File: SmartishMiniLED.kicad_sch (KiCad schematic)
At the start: 35 parts, among them J1 USB_C_Receptacle_USB2.0, J2 BUTTON, J3 Screw_Terminal_01x03, P1 NeopixelStripPads, P2 NeopixelStripPads, Q1 MMBT2222, Q2 MMBT2222, Q3 IRLML6344, Q4 IRF7410, SW2 TL3342, U1 ESP32-PICO-D4, U2 AP2112K-3.3, U3 CH340C, U4 74LVC1G125, U5 TSOP382xx

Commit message: Added some pads on the back for as an alternative to supplying the main power.
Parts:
- added J4: Conn_01x02, SmartishMiniLED:Main_Power, symbol Connector_Generic:Conn_01x02
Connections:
- net GND: now also J4.2 (Pin_2)
- net +5V_In: now reaches F1.1, J1.A4 (VBUS), J1.A9 (VBUS), J1.B4 (VBUS), J1.B9 (VBUS)
- net +5V_In: now also J4.1 (Pin_1)
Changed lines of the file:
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@@
+    (stroke (width 0) (type default) (color 0 0 0 0))
+  )
+  (wire (pts (xy 49.53 38.1) (xy 49.53 48.26))
     (stroke (width 0) (type default) (color 0 0 0 0))
   )
@@
     (stroke (width 0) (type default) (color 0 0 0 0))
   )
-  (wire (pts (xy 39.37 44.45) (xy 39.37 48.26))
-    (stroke (width 0) (type default) (color 0 0 0 0))
-  )
-  (wire (pts (xy 39.37 29.21) (xy 39.37 26.67))
+  (wire (pts (xy 30.48 45.72) (xy 30.48 49.53))
+    (stroke (width 0) (type default) (color 0 0 0 0))
+  )
+  (wire (pts (xy 30.48 30.48) (xy 30.48 27.94))
     (stroke (width 0) (type default) (color 0 0 0 0))
   )
@@
     (stroke (width 0) (type default) (color 0 0 0 0))
   )
+  (wire (pts (xy 49.53 35.56) (xy 46.99 35.56))
+    (stroke (width 0) (type default) (color 0 0 0 0))
+  )
   (wire (pts (xy 141.605 115.57) (xy 141.605 119.38))
     (stroke (width 0) (type default) (color 0 0 0 0))
   )
-  (wire (pts (xy 29.21 25.4) (xy 29.21 29.21))
+  (wire (pts (xy 20.32 26.67) (xy 20.32 30.48))
     (stroke (width 0) (type default) (color 0 0 0 0))
   )
@@
     (stroke (width 0) (type default) (color 0 0 0 0))
   )
+  (wire (pts (xy 46.99 38.1) (xy 49.53 38.1))
+    (stroke (width 0) (type default) (color 0 0 0 0))
+  )
   (wire (pts (xy 128.27 149.86) (xy 128.27 148.59))
     (stroke (width 0) (type default) (color 0 0 0 0))
@@
   )
   (wire (pts (xy 210.82 133.35) (xy 210.82 135.89))
+    (stroke (width 0) (type default) (color 0 0 0 0))
+  )
+  (wire (pts (xy 49.53 26.67) (xy 49.53 35.56))
     (stroke (width 0) (type default) (color 0 0 0 0))
   )
@@
   (label "RESET" (at 27.94 86.36 180)
     (effects (font (size 1.27 1.27)) (justify right bottom))
+  )
+  (label "+5V_In" (at 49.53 26.67 90)
+    (effects (font (size 1.27 1.27)) (justify left bottom))
+  )
+  (label "+5V_In" (at 201.93 115.57 90)
+    (effects (font (size 1.27 1.27)) (justify left bottom))
   )
   (label "DATA_OUT" (at 223.52 80.01 180)
@@
     (pin "1")
   )
-  (symbol (lib_id "power:PWR_FLAG") (at 39.37 29.21 180) (unit 1)
-    (in_bom yes) (on_board yes)
-    (property "Reference" "#FLG0101" (id 0) (at 39.37 31.115 0)
-      (effects (font (size 1.27 1.27)) hide)
-    )
-    (property "Value" "PWR_FLAG" (id 1) (at 39.37 33.6042 0))
-    (property "Footprint" "" (id 2) (at 39.37 29.21 0)
-      (effects (font (size 1.27 1.27)) hide)
-    )
-    (property "Datasheet" "~" (id 3) (at 39.37 29.21 0)
+  (symbol (lib_id "power:PWR_FLAG") (at 30.48 30.48 180) (unit 1)
+    (in_bom yes) (on_board yes)
+    (property "Reference" "#FLG0101" (id 0) (at 30.48 32.385 0)
+      (effects (font (size 1.27 1.27)) hide)
+    )
+    (property "Value" "PWR_FLAG" (id 1) (at 30.48 34.8742 0))
+    (property "Footprint" "" (id 2) (at 30.48 30.48 0)
+      (effects (font (size 1.27 1.27)) hide)
+    )
+    (property "Datasheet" "~" (id 3) (at 30.48 30.48 0)
       (effects (font (size 1.27 1.27)) hide)
     )
@@
     (pin "1")
   )
-  (symbol (lib_id "power:PWR_FLAG") (at 39.37 44.45 0) (unit 1)
-    (in_bom yes) (on_board yes)
-    (property "Reference" "#FLG0102" (id 0) (at 39.37 42.545 0)
-      (effects (font (size 1.27 1.27)) hide)
-    )
-    (property "Value" "PWR_FLAG" (id 1) (at 39.37 40.0558 0))
-    (property "Footprint" "" (id 2) (at 39.37 44.45 0)
-      (effects (font (size 1.27 1.27)) hide)
-    )
-    (property "Datasheet" "~" (id 3) (at 39.37 44.45 0)
-      (effects (font (size 1.27 1.27)) hide)
-    )
-    (pin "1")
-  )
-  (symbol (lib_id "power:GND") (at 39.37 48.26 0) (unit 1)
-    (in_bom yes) (on_board yes)
-    (property "Reference" "#PWR0123" (id 0) (at 39.37 54.61 0)
-      (effects (font (size 1.27 1.27)) hide)
-    )
-    (property "Value" "GND" (id 1) (at 39.497 52.6542 0))
-    (property "Footprint" "" (id 2) (at 39.37 48.26 0)
-      (effects (font (size 1.27 1.27)) hide)
-    )
-    (property "Datasheet" "" (id 3) (at 39.37 48.26 0)
+  (symbol (lib_id "power:PWR_FLAG") (at 30.48 45.72 0) (unit 1)
+    (in_bom yes) (on_board yes)
+    (property "Reference" "#FLG0102" (id 0) (at 30.48 43.815 0)
+      (effects (font (size 1.27 1.27)) hide)
+    )
+    (property "Value" "PWR_FLAG" (id 1) (at 30.48 41.3258 0))
+    (property "Footprint" "" (id 2) (at 30.48 45.72 0)
+      (effects (font (size 1.27 1.27)) hide)
+    )
+    (property "Datasheet" "~" (id 3) (at 30.48 45.72 0)
+      (effects (font (size 1.27 1.27)) hide)
+    )
+    (pin "1")
+  )
+  (symbol (lib_id "power:GND") (at 30.48 49.53 0) (unit 1)
+    (in_bom yes) (on_board yes)
+    (property "Reference" "#PWR0123" (id 0) (at 30.48 55.88 0)
+      (effects (font (size 1.27 1.27)) hide)
+    )
+    (property "Value" "GND" (id 1) (at 30.607 53.9242 0))
+    (property "Footprint" "" (id 2) (at 30.48 49.53 0)
+      (effects (font (size 1.27 1.27)) hide)
+    )
+    (property "Datasheet" "" (id 3) (at 30.48 49.53 0)
       (effects (font (size 1.27 1.27)) hide)
     )
@@
     (pin "1")
   )
-  (symbol (lib_id "power:PWR_FLAG") (at 29.21 29.21 180) (unit 1)
-    (in_bom yes) (on_board yes)
-    (property "Reference" "#FLG01" (id 0) (at 29.21 31.115 0)
-      (effects (font (size 1.27 1.27)) hide)
-    )
-    (property "Value" "PWR_FLAG" (id 1) (at 29.21 33.6042 0))
-    (property "Footprint" "" (id 2) (at 29.21 29.21 0)
-      (effects (font (size 1.27 1.27)) hide)
-    )
-    (property "Datasheet" "~" (id 3) (at 29.21 29.21 0)
+  (symbol (lib_id "power:PWR_FLAG") (at 20.32 30.48 180) (unit 1)
+    (in_bom yes) (on_board yes)
+    (property "Reference" "#FLG01" (id 0) (at 20.32 32.385 0)
+      (effects (font (size 1.27 1.27)) hide)
+    )
+    (property "Value" "PWR_FLAG" (id 1) (at 20.32 34.8742 0))
+    (property "Footprint" "" (id 2) (at 20.32 30.48 0)
+      (effects (font (size 1.27 1.27)) hide)
+    )
+    (property "Datasheet" "~" (id 3) (at 20.32 30.48 0)
       (effects (font (size 1.27 1.27)) hide)
     )
@@
     (pin "1")
   )
-  (symbol (lib_id "power:VBUS") (at 39.37 26.67 0) (unit 1)
-    (in_bom yes) (on_board yes)
-    (property "Reference" "#PWR0113" (id 0) (at 39.37 30.48 0)
-      (effects (font (size 1.27 1.27)) hide)
-    )
-    (property "Value" "VBUS" (id 1) (at 39.751 22.2758 0))
-    (property "Footprint" "" (id 2) (at 39.37 26.67 0)
-      (effects (font (size 1.27 1.27)) hide)
-    )
-    (property "Datasheet" "" (id 3) (at 39.37 26.67 0)
+  (symbol (lib_id "Connector_Generic:Conn_01x02") (at 41.91 35.56 0) (mirror y) (unit 1)
+    (in_bom yes) (on_board yes) (fields_autoplaced)
+    (property "Reference" "J4" (id 0) (at 41.91 29.21 0))
+    (property "Value" "Conn_01x02" (id 1) (at 41.91 31.75 0))
+    (property "Footprint" "SmartishMiniLED:Main_Power" (id 2) (at 41.91 35.56 0)
+      (effects (font (size 1.27 1.27)) hide)
+    )
+    (property "Datasheet" "~" (id 3) (at 41.91 35.56 0)
+      (effects (font (size 1.27 1.27)) hide)
+    )
+    (pin "1")
+    (pin "2")
+  )
+  (symbol (lib_id "power:VBUS") (at 30.48 27.94 0) (unit 1)
+    (in_bom yes) (on_board yes)
+    (property "Reference" "#PWR0113" (id 0) (at 30.48 31.75 0)
+      (effects (font (size 1.27 1.27)) hide)
+    )
+    (property "Value" "VBUS" (id 1) (at 30.861 23.5458 0))
+    (property "Footprint" "" (id 2) (at 30.48 27.94 0)
+      (effects (font (size 1.27 1.27)) hide)
+    )
+    (property "Datasheet" "" (id 3) (at 30.48 27.94 0)
       (effects (font (size 1.27 1.27)) hide)
     )
@@
     (pin "1")
   )
-  (symbol (lib_id "power:+5V") (at 29.21 25.4 0) (unit 1)
-    (in_bom yes) (on_board yes)
-    (property "Reference" "#PWR03" (id 0) (at 29.21 29.21 0)
-      (effects (font (size 1.27 1.27)) hide)
-    )
-    (property "Value" "+5V" (id 1) (at 29.591 22.1488 0)
-      (effects (font (size 1.27 1.27)) (justify left))
-    )
-    (property "Footprint" "" (id 2) (at 29.21 25.4 0)
-      (effects (font (size 1.27 1.27)) hide)
-    )
-    (property "Datasheet" "" (id 3) (at 29.21 25.4 0)
+  (symbol (lib_id "power:+5V") (at 20.32 26.67 0) (unit 1)
+    (in_bom yes) (on_board yes)
+    (property "Reference" "#PWR03" (id 0) (at 20.32 30.48 0)
+      (effects (font (size 1.27 1.27)) hide)
+    )
+    (property "Value" "+5V" (id 1) (at 20.701 23.4188 0)
+      (effects (font (size 1.27 1.27)) (justify left))
+    )
+    (property "Footprint" "" (id 2) (at 20.32 26.67 0)
+      (effects (font (size 1.27 1.27)) hide)
+    )
+    (property "Datasheet" "" (id 3) (at 20.32 26.67 0)
       (effects (font (size 1.27 1.27)) hide)
     )
@@
     (pin "3")
   )
+  (symbol (lib_id "power:GND") (at 49.53 48.26 0) (unit 1)
+    (in_bom yes) (on_board yes)
+    (property "Reference" "#PWR0102" (id 0) (at 49.53 54.61 0)
+      (effects (font (size 1.27 1.27)) hide)
+    )
+    (property "Value" "GND" (id 1) (at 49.657 52.6542 0))
+    (property "Footprint" "" (id 2) (at 49.53 48.26 0)
+      (effects (font (size 1.27 1.27)) hide)
+    )
+    (property "Datasheet" "" (id 3) (at 49.53 48.26 0)
+      (effects (font (size 1.27 1.27)) hide)
+    )
+    (pin "1")
+  )
   (symbol (lib_id "power:GND") (at 78.105 186.69 0) (unit 1)
     (in_bom yes) (on_board yes)
@@
       (reference "#PWR0101") (unit 1) (value "VBUS") (footprint "")
     )
+    (path "/b0a94077-f2a4-4a3d-bb66-8b20639c041a"
+      (reference "#PWR0102") (unit 1) (value "GND") (footprint "")
+    )
     (path "/00000000-0000-0000-0000-00005f9e862a"
       (reference "#PWR0104") (unit 1) (value "GND") (footprint "")
@@
       (reference "J3") (unit 1) (value "Screw_Terminal_01x03") (footprint "TerminalBlock_TE-Connectivity:TerminalBlock_TE_282834-3_1x03_P2.54mm_Horizontal")
     )
+    (path "/2ffa9763-7cd5-4d26-a22c-2fbedca8ab30"
+      (reference "J4") (unit 1) (value "Conn_01x02") (footprint "SmartishMiniLED:Main_Power")
+    )
     (path "/9a6db930-05fd-4343-b34b-d17254368269"

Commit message: Updates for production
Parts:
- R2, R3: LCSC C17414 -> C17617
- R7: footprint Resistor_SMD:R_0805_2012Metric_Pad1.20x1.40mm_HandSolder -> Resistor_SMD:R_0805_2012Metric
- R8, R9: value 10k -> 10K; footprint Resistor_SMD:R_0805_2012Metric_Pad1.20x1.40mm_HandSolder -> Resistor_SMD:R_0805_2012Metric
- U4: LCSC C12518 -> C17724
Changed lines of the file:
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@@
       (effects (font (size 1.27 1.27)) hide)
     )
-    (property "LCSC" "C17414" (id 4) (at 106.68 154.94 0)
+    (property "LCSC" "C17617" (id 4) (at 106.68 154.94 0)
       (effects (font (size 1.27 1.27)) hide)
     )
@@
       (effects (font (size 1.27 1.27)) hide)
     )
-    (property "LCSC" "C17414" (id 4) (at 106.68 176.53 0)
+    (property "LCSC" "C17617" (id 4) (at 106.68 176.53 0)
       (effects (font (size 1.27 1.27)) hide)
     )
@@
       (effects (font (size 1.27 1.27)) (justify left))
     )
-    (property "Footprint" "Resistor_SMD:R_0805_2012Metric_Pad1.20x1.40mm_HandSolder" (id 2) (at 104.775 117.602 90)
+    (property "Footprint" "Resistor_SMD:R_0805_2012Metric" (id 2) (at 104.775 117.602 90)
       (effects (font (size 1.27 1.27)) hide)
     )
@@
       (effects (font (size 1.27 1.27)) (justify left))
     )
-    (property "Value" "10k" (id 1) (at 124.46 104.775 90)
-      (effects (font (size 1.27 1.27)) (justify left))
-    )
-    (property "Footprint" "Resistor_SMD:R_0805_2012Metric_Pad1.20x1.40mm_HandSolder" (id 2) (at 122.682 102.87 90)
+    (property "Value" "10K" (id 1) (at 124.46 104.775 90)
+      (effects (font (size 1.27 1.27)) (justify left))
+    )
+    (property "Footprint" "Resistor_SMD:R_0805_2012Metric" (id 2) (at 122.682 102.87 90)
       (effects (font (size 1.27 1.27)) hide)
     )
@@
       (effects (font (size 1.27 1.27)) (justify left))
     )
-    (property "Value" "10k" (id 1) (at 112.395 127.635 90)
-      (effects (font (size 1.27 1.27)) (justify left))
-    )
-    (property "Footprint" "Resistor_SMD:R_0805_2012Metric_Pad1.20x1.40mm_HandSolder" (id 2) (at 110.617 125.73 90)
+    (property "Value" "10K" (id 1) (at 112.395 127.635 90)
+      (effects (font (size 1.27 1.27)) (justify left))
+    )
+    (property "Footprint" "Resistor_SMD:R_0805_2012Metric" (id 2) (at 110.617 125.73 90)
       (effects (font (size 1.27 1.27)) hide)
     )
@@
       (effects (font (size 1.27 1.27)) hide)
     )
-    (property "LCSC" "C12518" (id 4) (at 129.54 76.2 0)
+    (property "LCSC" "C17724" (id 4) (at 129.54 76.2 0)
       (effects (font (size 1.6002 1.6002)) hide)
     )
@@
     )
     (path "/435d05df-49ce-4cfa-ba0f-5bb784df8509"
-      (reference "R7") (unit 1) (value "300R") (footprint "Resistor_SMD:R_0805_2012Metric_Pad1.20x1.40mm_HandSolder")
+      (reference "R7") (unit 1) (value "300R") (footprint "Resistor_SMD:R_0805_2012Metric")
     )
     (path "/70ff8a3e-79f3-4c05-959b-a0864d858be3"
-      (reference "R8") (unit 1) (value "10k") (footprint "Resistor_SMD:R_0805_2012Metric_Pad1.20x1.40mm_HandSolder")
+      (reference "R8") (unit 1) (value "10K") (footprint "Resistor_SMD:R_0805_2012Metric")
     )
     (path "/6cd4d330-3e90-41f4-9bea-27d72eabc203"
-      (reference "R9") (unit 1) (value "10k") (footprint "Resistor_SMD:R_0805_2012Metric_Pad1.20x1.40mm_HandSolder")
+      (reference "R9") (unit 1) (value "10K") (footprint "Resistor_SMD:R_0805_2012Metric")
     )
     (path "/00000000-0000-0000-0000-00005fb40bf2"

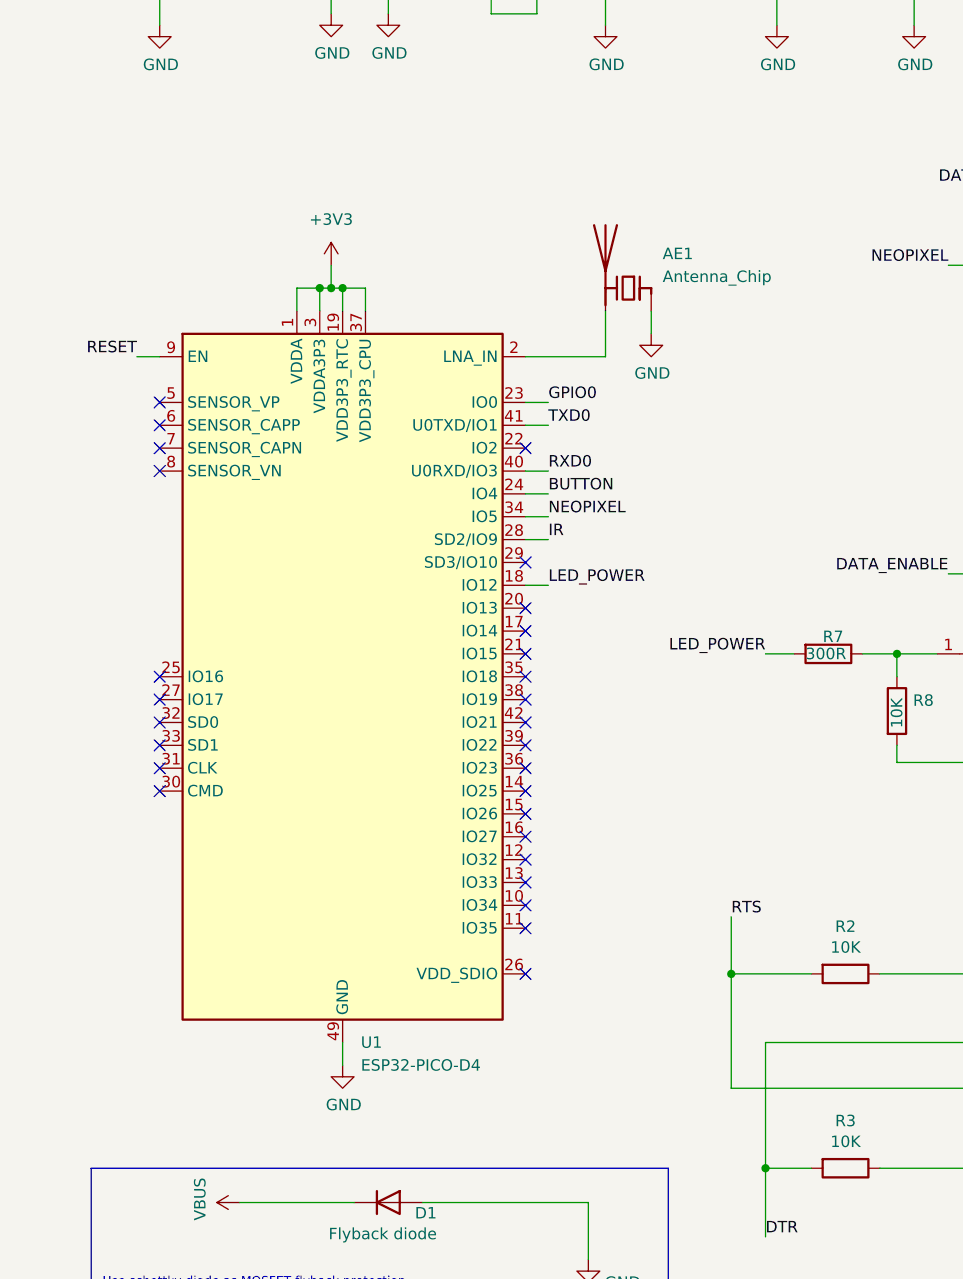
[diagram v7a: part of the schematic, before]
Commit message: Reworked using the WROOM-32D module
This allows for easier manufacrure
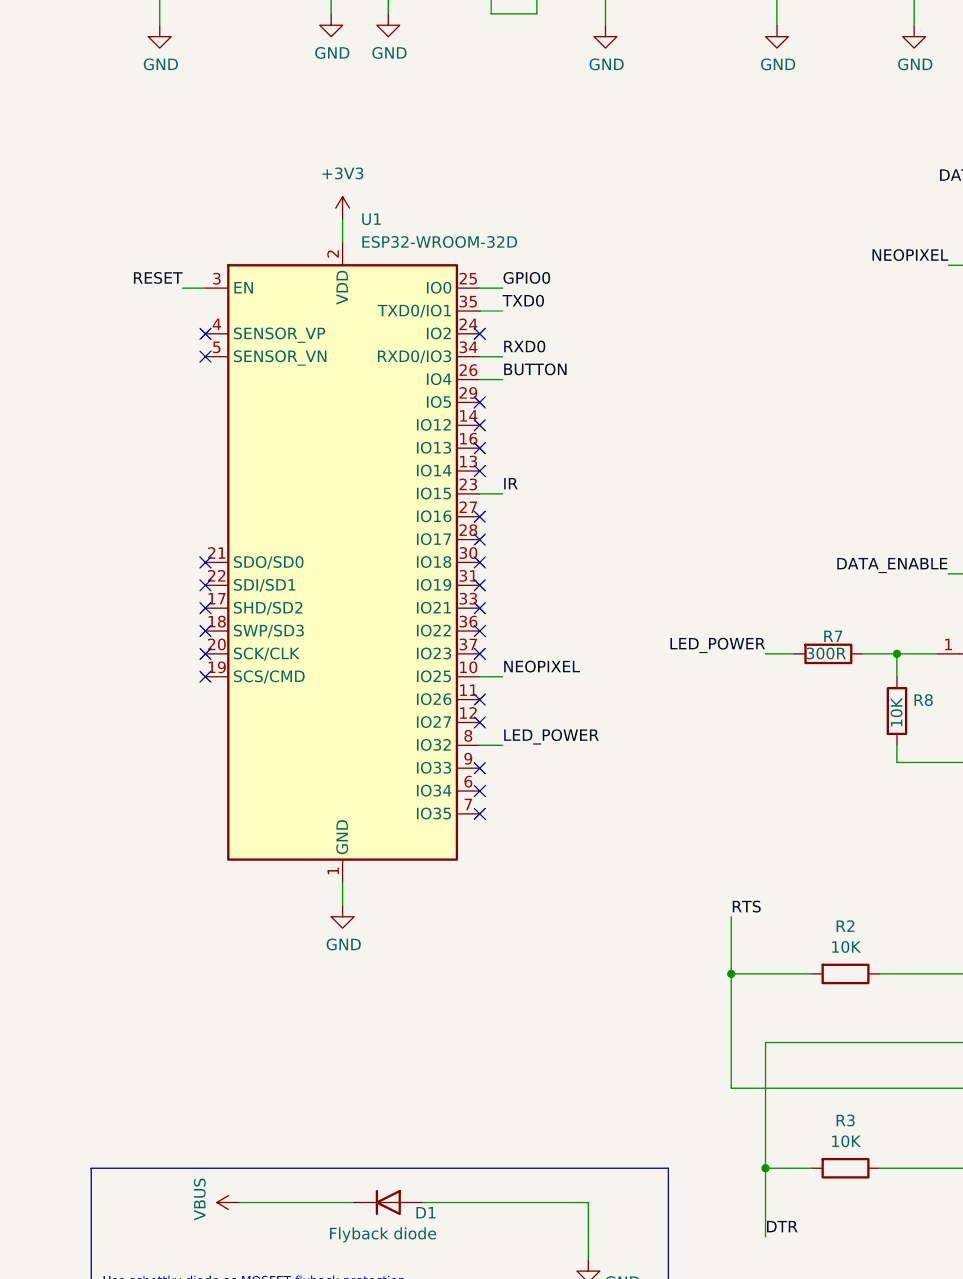
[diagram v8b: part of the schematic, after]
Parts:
- removed AE1: Antenna_Chip, SmartishMiniLED:Texas_SWRA117D_2.4GHz_Right, symbol Device:Antenna_Chip
- removed U1: ESP32-PICO-D4, Package_DFN_QFN:QFN-48-1EP_7x7mm_P0.5mm_EP5.3x5.3mm, symbol RF_Module:ESP32-PICO-D4
- added U1: ESP32-WROOM-32D, RF_Module:ESP32-WROOM-32, symbol RF_Module:ESP32-WROOM-32D
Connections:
- net +3V3: now also U1.2 (VDD)
- net BUTTON: now also U1.26 (IO4)
- net GND: now also U1.1 (GND), U1.15 (GND), U1.38 (GND), U1.39 (GND)
- net GPIO0: now also U1.25 (IO0)
- net IR: now also U1.23 (IO15)
- net LED_POWER: now also U1.8 (IO32)
- net NEOPIXEL: now also U1.10 (IO25)
- net RESET: now also U1.3 (EN)
- net RXD0: now also U1.34 (RXD0/IO3)
- net TXD0: now also U1.35 (TXD0/IO1)
- no-connect marks 35 -> 32
